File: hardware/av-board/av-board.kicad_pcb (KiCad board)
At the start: 4 copper layers, 94.6 x 69.4 mm, 219 parts, among them J1 RCA Y, J10 2x20 socket, J2 RCA Pb, J3 RCA Pr, J4 RCA L, J5 RCA R, J6 HDMI-001, J9 2x20 socket, SW1 TS-1187A-B-A-B, SW2 TS-1187A-B-A-B, U1 ADV7842KBCZ-5, U10 TPD4E05U06DQAR, U2 ADV7511KSTZ, U3 PCM1808PWR, U4 TLV62569DBVR, U5 TPS7A7001DDAR, U6 TPS7A7001DDAR, U7 TPS7A7001DDAR, U8 TPD4E05U06DQAR, U9 TPD4E05U06DQAR, Y1 28.63636MHz 20pF

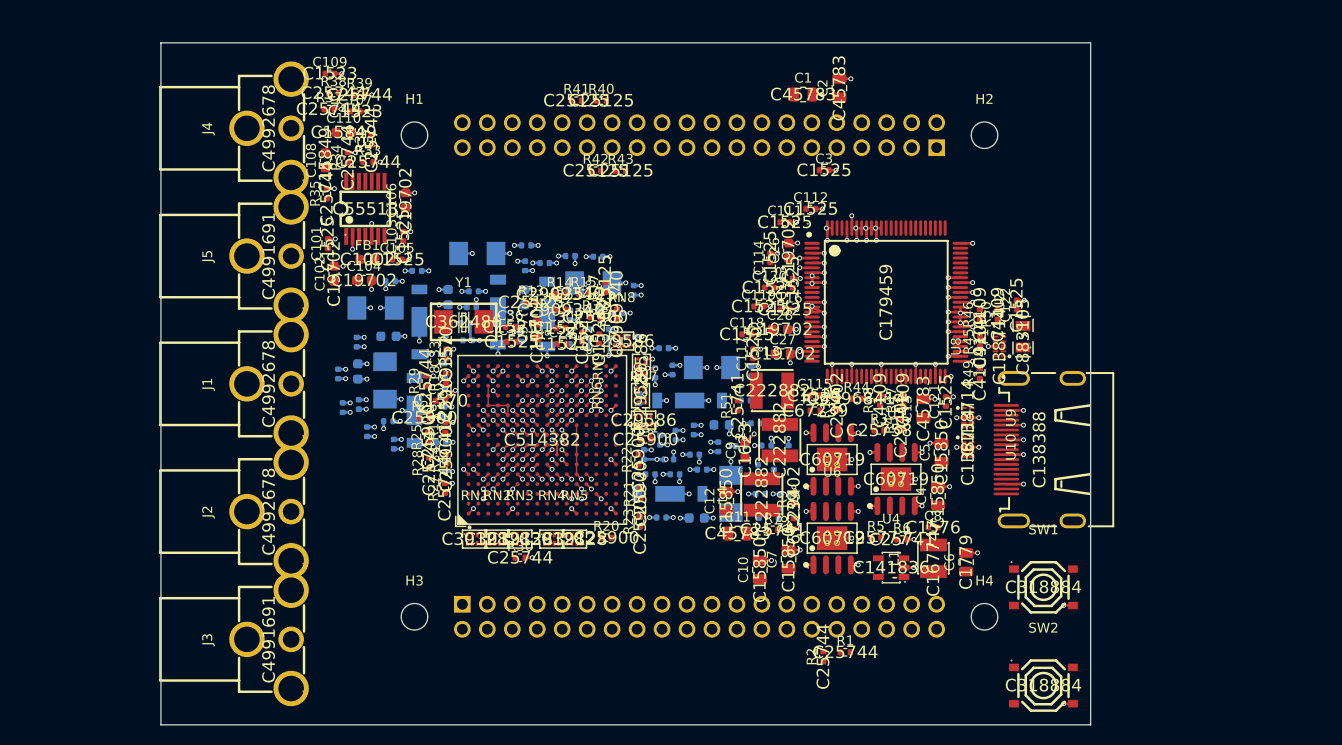
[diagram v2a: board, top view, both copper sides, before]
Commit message: Review against the data sheets: LDO feed-forward and EN, HPD, anti-alias, clock clearance
Every IC checked pin by pin against its document (design.md "Review against the data sheets"):
the ADV7842 against every row of UG-214 App. C and the AIN_SEL routing, the ADV7511 against
HWG Rev D, the PCM1808, TPS7A7001, TLV62569 and TPD4E05U06 against their data sheets. Fixed:

- TPS7A7001: a 220 pF feed-forward across R1 on all three; the data sheet requires it with
  47-200 uF on the output (3V3 and both 1.8 V rails carry more than 47 uF through the filters).
  U6/U7 output 22 uF -> 10 uF, keeping 1V8A (about 185 uF) under the 200 uF limit.
- TPS7A7001 EN: the 1.8 V LDOs' enable RC now pulls up to 2V5, their VIN; from 3V3 it put EN
  above VIN (recommended: EN <= VIN). The 1.8 V rails still come up about 30 ms after 2V5.
- ADV7511 HPD: 10 k to GND as HWG 6.1.4 asks (was 100 k).
- PCM1808 anti-alias cap 220 pF (145 kHz, TI's range); the 1 nF cut 1.4 dB at 20 kHz.
- A CLOCK netclass (OUT_CLK, LLC) with 0.19 mm clearance, what the 0.5 mm-pitch pads allow
  (HWG 7.2: nothing near the CLK trace).

ERC clean, schematic = board.py (903 pins), DRC: only the unrouted connections.

Co-Authored-By: Claude Opus 5.5 <noreply@anthropic.com>
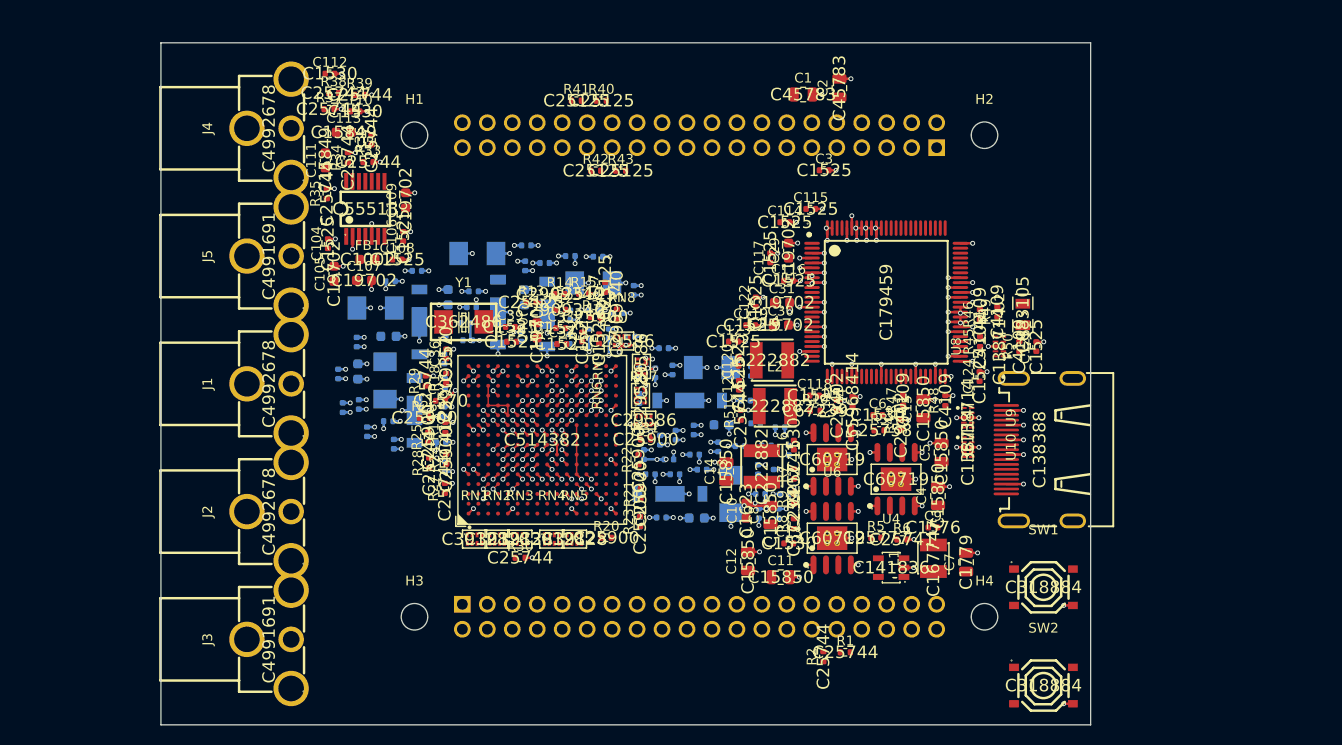
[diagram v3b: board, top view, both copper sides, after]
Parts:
- added C123: 100n, Capacitor_SMD:C_0402_1005Metric, F.Cu at (132.4, 51.0)
- added C124: 100n, Capacitor_SMD:C_0402_1005Metric, F.Cu at (157.5, 54.5)
- added C125: 100n, Capacitor_SMD:C_0402_1005Metric, F.Cu at (163.3, 51.5)
- C10: value 10u -> 470n; footprint Capacitor_SMD:C_0805_2012Metric -> Capacitor_SMD:C_0603_1608Metric
- C100, C112: value 100n -> 220p
- C101: value 100n -> 220p; moved to B.Cu
- C102: value 10u -> 10n; footprint Capacitor_SMD:C_0603_1608Metric -> Capacitor_SMD:C_0402_1005Metric; moved to B.Cu
- C103, C26, C28: moved to B.Cu
- C104, C106: value 10u -> 100n; footprint Capacitor_SMD:C_0603_1608Metric -> Capacitor_SMD:C_0402_1005Metric
- C105, C29, C30, C31: value 100n -> 10u; footprint Capacitor_SMD:C_0402_1005Metric -> Capacitor_SMD:C_0603_1608Metric
- C107, C109: value 1n -> 10u; footprint Capacitor_SMD:C_0402_1005Metric -> Capacitor_SMD:C_0603_1608Metric
- C108: value 1u -> 100n; footprint Capacitor_SMD:C_0603_1608Metric -> Capacitor_SMD:C_0402_1005Metric
- C11: value 22u -> 10u
- C110: value 1u -> 220p; footprint Capacitor_SMD:C_0603_1608Metric -> Capacitor_SMD:C_0402_1005Metric
- C111, C113: value 100n -> 1u; footprint Capacitor_SMD:C_0402_1005Metric -> Capacitor_SMD:C_0603_1608Metric
- C13: value 22u -> 220p; footprint Capacitor_SMD:C_0805_2012Metric -> Capacitor_SMD:C_0402_1005Metric
- C14: value 33u -> 10u; footprint lcsc:CAP-SMD_L3.5-W2.8-R-RD -> Capacitor_SMD:C_0805_2012Metric; moved to F.Cu
- C15: footprint Capacitor_SMD:C_0603_1608Metric -> Capacitor_SMD:C_0805_2012Metric; moved to F.Cu
- C16: value 33u -> 220p; footprint lcsc:CAP-SMD_L3.5-W2.8-R-RD -> Capacitor_SMD:C_0402_1005Metric; moved to F.Cu
- C17, C19, C21, C23, C25: value 10u -> 33u; footprint Capacitor_SMD:C_0603_1608Metric -> lcsc:CAP-SMD_L3.5-W2.8-R-RD
- C18, C20, C22, C24: value 33u -> 10u; footprint lcsc:CAP-SMD_L3.5-W2.8-R-RD -> Capacitor_SMD:C_0603_1608Metric
- C27: value 10u -> 33u; footprint Capacitor_SMD:C_0603_1608Metric -> lcsc:CAP-SMD_L3.5-W2.8-R-RD; moved to B.Cu
- C32: value 1n -> 100n
- C33, C34: value 30p -> 100n
- C35: value 100n -> 1n
- C36: value 100n -> 30p
- C37: value 10u -> 30p; footprint Capacitor_SMD:C_0603_1608Metric -> Capacitor_SMD:C_0402_1005Metric
- C38, C39: value 10n -> 100n; moved to F.Cu
- C40: value 100n -> 10u; footprint Capacitor_SMD:C_0402_1005Metric -> Capacitor_SMD:C_0603_1608Metric; moved to F.Cu
- C41, C68: value 100n -> 10n
- C42, C56, C57, C58, C74, C75, C86, C87, C88: value 220p -> 10n
- C43, C44: value 220p -> 100n
- C51, C52, C53, C65, C66, C67, C77, C78, C99: value 10n -> 220p
- C6: value 4.7u -> 220p; footprint Capacitor_SMD:C_0805_2012Metric -> Capacitor_SMD:C_0402_1005Metric
- C7: value 10u -> 4.7u
- C71: value 10n -> 100n
- C8: value 6.8p -> 10u; footprint Capacitor_SMD:C_0402_1005Metric -> Capacitor_SMD:C_0805_2012Metric
- C9: value 470n -> 6.8p; footprint Capacitor_SMD:C_0603_1608Metric -> Capacitor_SMD:C_0402_1005Metric
- R51: value 100k -> 10k
- moved C101 51.4 mm to (138.1, 62.1)
- moved C112 50.8 mm to (91.4, 23.7)
- moved C113 48.2 mm to (92.8, 29.7), turned to 0 degrees
- moved C111 47.2 mm to (90.9, 32.6), turned to 90 degrees
- moved C28 43.2 mm to (94.2, 54.0), turned to 90 degrees
- moved C27 41.7 mm to (96.0, 47.6)
- moved C25 40.0 mm to (132.2, 66.5)
- moved C22 38.4 mm to (97.4, 50.5), turned to 0 degrees
- moved C99 37.1 mm to (137.7, 66.5)
- moved C23 35.0 mm to (106.4, 42.0)
- moved C18 34.5 mm to (131.2, 59.5), turned to 0 degrees
- moved C100 34.1 mm to (137.2, 59.7)
- moved C26 28.8 mm to (128.7, 69.0), turned to 0 degrees
- moved C122 26.6 mm to (134.7, 47.0)
- moved C16 26.2 mm to (138.6, 61.5), turned to 90 degrees
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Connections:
- C10 pad 1: 2V5 -> EN_1V8
- C100 pad 1: AV_PVDD -> AV_DVDDIO
- C101 pad 1: VREF -> AV_DVDDIO
- C102 pad 1: VREF -> AV_PVDD
- C103 pad 1: 5VA -> AV_PVDD
- C104 pad 1: 5VA -> VREF
- C105 pad 1: 3V3 -> VREF
- C106 pad 1: 3V3 -> 5VA
- C107 pad 1: AUD_DIV_L -> 5VA
- C108 pad 1: AUD_DIV_L -> 3V3
- C108 pad 2: AUD_VINL -> GND
- C109 pad 1: AUD_DIV_R -> 3V3
- C11 pad 1: 1V8A -> 2V5
- C110 pad 1: AUD_DIV_R -> AUD_DIV_L
- C110 pad 2: AUD_VINR -> GND
- C111 pad 1: TX_DVDD -> AUD_DIV_L
- C111 pad 2: GND -> AUD_VINL
- C112 pad 1: TX_DVDD -> AUD_DIV_R
- C113 pad 1: TX_DVDD -> AUD_DIV_R
- C113 pad 2: GND -> AUD_VINR
- C115 pad 1: TX_AVDD -> TX_DVDD
- C116 pad 1: TX_AVDD -> TX_DVDD
- C117 pad 1: TX_AVDD -> TX_DVDD
- C119 pad 1: TX_PLVDD -> TX_AVDD
- C12 pad 1: 2V5 -> 1V8A
- C120 pad 1: TX_PLVDD -> TX_AVDD
- C121 pad 1: 3V3 -> TX_AVDD
- C122 pad 1: HDMI_5V -> TX_PLVDD
- C13 pad 1: 1V8B -> 1V8A
- C13 pad 2: GND -> FB_1V8A
- C14 pad 1: AV_VDD -> 2V5
- C15 pad 1: AV_VDD -> 1V8B
- C16 pad 1: AV_AVDD -> 1V8B
- C16 pad 2: GND -> FB_1V8B
- C17 pad 1: AV_AVDD -> AV_VDD
- C18 pad 1: AV_CVDD -> AV_VDD
- C19 pad 1: AV_CVDD -> AV_AVDD
- C20 pad 1: AV_PVDD -> AV_AVDD
- C21 pad 1: AV_PVDD -> AV_CVDD
- C22 pad 1: AV_DVDDIO -> AV_CVDD
- C23 pad 1: AV_DVDDIO -> AV_PVDD
- C24 pad 1: AV_TVDD -> AV_PVDD
- C25 pad 1: AV_TVDD -> AV_DVDDIO
- C26 pad 1: TX_DVDD -> AV_DVDDIO
- C27 pad 1: TX_AVDD -> AV_TVDD
- C28 pad 1: TX_PLVDD -> AV_TVDD
- C29 pad 1: TERM_Y -> TX_DVDD
- C29 pad 2: AIN_Y -> GND
- C30 pad 1: TERM_PB -> TX_AVDD
- C30 pad 2: AIN_PB -> GND
- C31 pad 1: TERM_PR -> TX_PLVDD
- C31 pad 2: AIN_PR -> GND
- C32 pad 2: SYNC_Y -> AIN_Y
- C33 pad 1: XTALP -> TERM_PB
- C33 pad 2: GND -> AIN_PB
- C34 pad 1: XTALN -> TERM_PR
- C34 pad 2: GND -> AIN_PR
- C35 pad 1: REFP -> TERM_Y
- C35 pad 2: GND -> SYNC_Y
- C36 pad 1: REFN -> XTALP
- C37 pad 1: REFP -> XTALN
- C37 pad 2: REFN -> GND
- C38 pad 1: AV_TVDD -> REFP
- C39 pad 1: AV_TVDD -> REFN
- C40 pad 1: AV_TVDD -> REFP
- C40 pad 2: GND -> REFN
- C51 pad 1: AV_AVDD -> AV_TVDD
- C52 pad 1: AV_AVDD -> AV_TVDD
- C53 pad 1: AV_AVDD -> AV_TVDD
- C6 pad 1: +5V -> 3V3
- C6 pad 2: GND -> FB_3V3
- C65 pad 1: AV_CVDD -> AV_AVDD
- C66 pad 1: AV_CVDD -> AV_AVDD
- C67 pad 1: AV_CVDD -> AV_AVDD
- C69 pad 1: AV_VDD -> AV_CVDD
- C7 pad 1: 2V5 -> +5V
- C70 pad 1: AV_VDD -> AV_CVDD
- C71 pad 1: AV_VDD -> AV_CVDD
- C76 pad 1: AV_DVDDIO -> AV_VDD
- C77 pad 1: AV_DVDDIO -> AV_VDD
- C78 pad 1: AV_DVDDIO -> AV_VDD
- C8 pad 2: FB_2V5 -> GND
- C9 pad 1: EN_1V8 -> 2V5
- C9 pad 2: GND -> FB_2V5
- C99 pad 1: AV_PVDD -> AV_DVDDIO
- R7 pad 1: 3V3 -> 2V5
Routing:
- net GND: track 243.9 -> 247.9 mm, vias 269 -> 271
- net AV_DVDDIO: track 25.6 -> 24.2 mm, vias 25 -> 24
- net AV_VDD: track 11.2 -> 12.0 mm, vias 13 -> 14

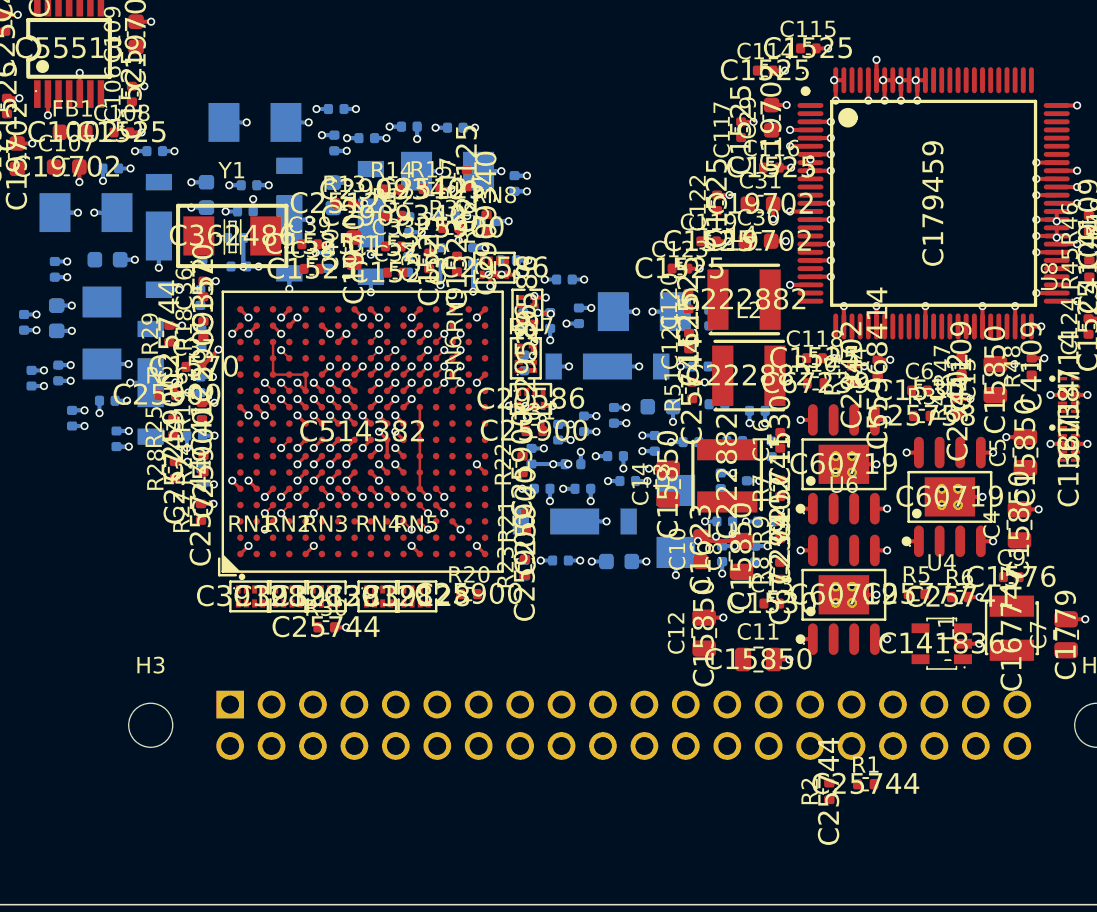
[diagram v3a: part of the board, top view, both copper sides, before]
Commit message: Routing room round the BGA, 6-layer stack, finishing pass after an outside router
What DeepPCB left open on four layers (14 of 743, no clearance errors or shorts) was nearly all
escapes from under the ADV7842: the SDRAM pull-down corner, two pixel lines, SYNC_Y and the two
RXA/RXB_5V balls. So:

- A 1 mm ring round the ADV7842 is kept free of small parts on both sides (its outer two rings
  escape through it), and the J10 bus's fan-out under the 75 R arrays is reserved for routing.
- RXA/RXB_5V take escape vias like the other inner balls (they had F.Cu only).
- Six layers: JLC06161H-7628B, whose outer prepreg (0.218 mm, er 4.4) keeps the TMDS geometry.
- route(): a session from elsewhere (DeepPCB, SES=) gets a Freerouting pass with its copper
  fixed, for what it left open (FINISH=0: none). Import, finish and pour run in processes of
  their own: after a DSN export pcbnew can no longer list a board's tracks or load a board.
- stitch() keeps out of the standoffs' 6 mm square keepouts (it used a 3 mm circle).
- snap.py: --clip to zoom, --layers; the outline comes from an Edge.Cuts-only plot.

Co-Authored-By: Claude Opus 5.5 <noreply@anthropic.com>
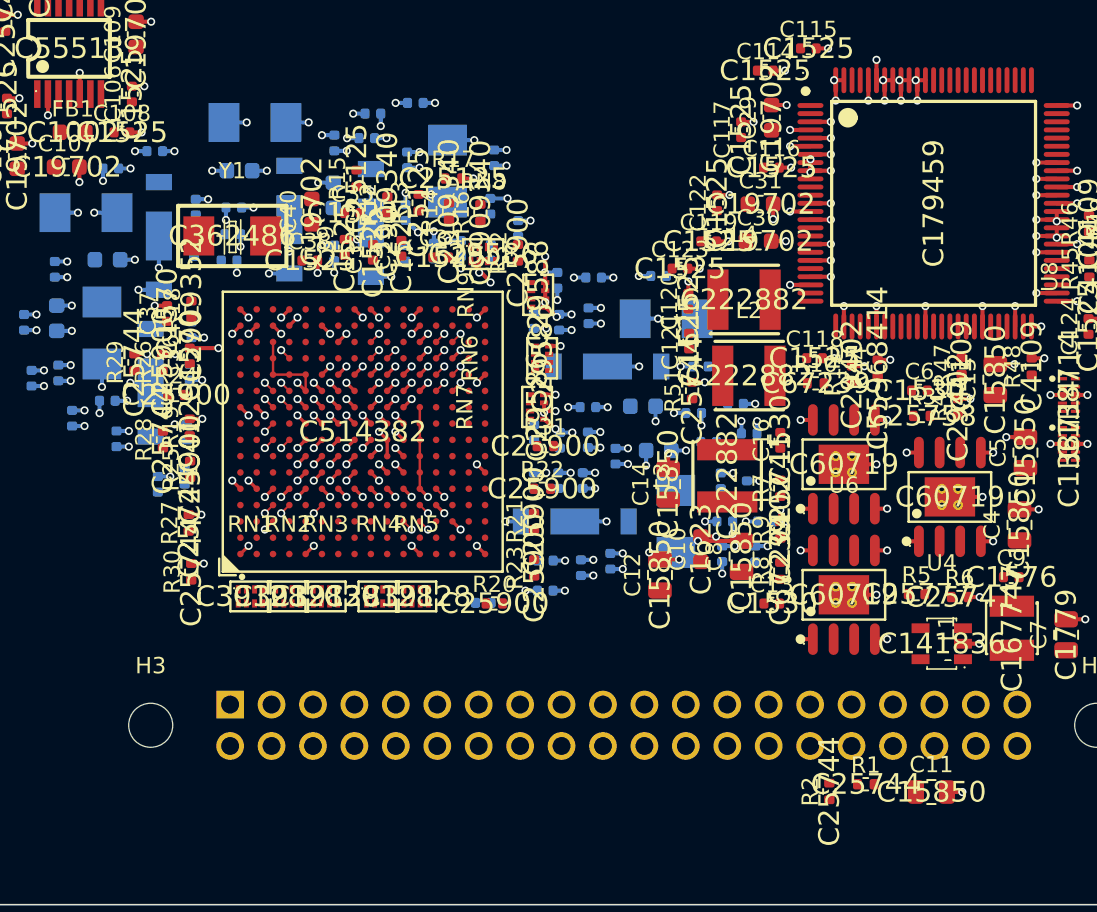
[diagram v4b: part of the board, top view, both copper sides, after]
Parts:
- moved C101 20.0 mm to (120.4, 71.5), turned to 0 degrees
- moved C100 17.1 mm to (124.2, 70.7)
- moved C71 15.8 mm to (100.4, 64.2), turned to 90 degrees
- moved C11 13.4 mm to (147.9, 83.1)
- moved C98 9.28 mm to (135.9, 59.3), turned to 0 degrees
- moved C64 9.14 mm to (122.5, 48.5), turned to 90 degrees
- moved R30 8.94 mm to (102.5, 69.6), turned to 90 degrees
- moved C67 7.84 mm to (116.2, 40.8), turned to 0 degrees
- moved C83 7.37 mm to (125.1, 61.5), turned to 90 degrees
- moved C26 7.23 mm to (131.1, 62.2)
- moved C35 7.14 mm to (112.4, 47.6), turned to 0 degrees
- moved C91 7.12 mm to (135.0, 68.5), turned to 90 degrees
- moved C96 7.03 mm to (137.1, 68.5), turned to 90 degrees
- moved C93 6.91 mm to (134.2, 61.6), turned to 0 degrees
- moved C92 6.91 mm to (133.3, 59.9)
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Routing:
- net AV_DVDDIO: track 24.2 -> 20.8 mm, vias 24 -> 21
- net GND: track 247.9 -> 249.6 mm, vias 271 -> 270
- net AV_AVDD: track 15.6 -> 14.1 mm, vias 18 -> 17
- net +5V: track 0.00 -> 1.41 mm, vias 0 -> 2
- net AV_TVDD: track 15.5 -> 14.7 mm, vias 19 -> 18
- net AV_PVDD: track 6.15 -> 5.72 mm, vias 7 -> 6
- net AV_VDD: track 12.0 -> 11.9 mm, vias 14 -> 15
